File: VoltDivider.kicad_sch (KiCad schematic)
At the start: 4 parts, among them J4 Conn_01x01_Female

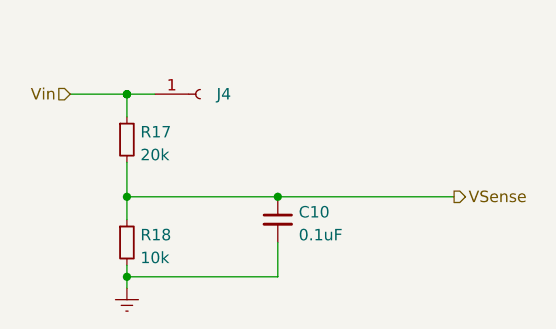
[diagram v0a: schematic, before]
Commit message: added new op amps and used automated traces due to complexity
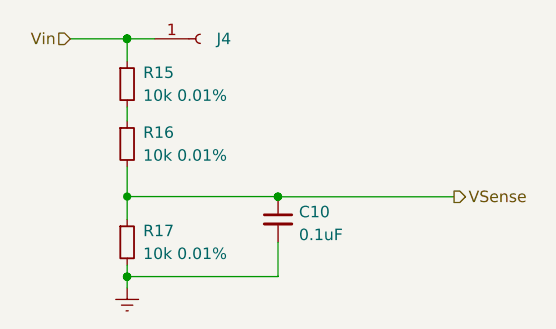
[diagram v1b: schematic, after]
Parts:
- added R16: 10k 0.01%, Resistor_SMD:R_0603_1608Metric, symbol Device:R_Small
- R15: renamed from R17; value 20k -> 10k 0.01%
- R17: renamed from R18; value 10k -> 10k 0.01%
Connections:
- net VSense: now also R16.2; no longer R15.2
- new net: R15.2, R16.1
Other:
- moved on the sheet: J4, R15
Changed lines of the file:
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@@
 (kicad_sch (version 20211123) (generator eeschema)
   (paper "A4")
-  (junction (at 134.0866 78.8162) (diameter 0) (color 0 0 0 0)
+  (junction (at 150.876 90.17) (diameter 0) (color 0 0 0 0)
   )
-  (junction (at 134.0866 90.1954) (diameter 0) (color 0 0 0 0)
+  (junction (at 134.0866 72.6694) (diameter 0) (color 0 0 0 0)
+  )
+  (junction (at 134.112 90.17) (diameter 0) (color 0 0 0 0)
   )
   (junction (at 134.0866 99.0854) (diameter 0) (color 0 0 0 0)
   )
-  (junction (at 134.0866 78.7908) (diameter 0) (color 0 0 0 0)
+  (junction (at 134.112 72.5932) (diameter 0) (color 0 0 0 0)
+  )
+  (junction (at 134.112 99.06) (diameter 0) (color 0 0 0 0)
+  )
+  (junction (at 134.0866 72.644) (diameter 0) (color 0 0 0 0)
   )
   (junction (at 150.8506 90.1954) (diameter 0) (color 0 0 0 0)
   )
-  (wire (pts (xy 134.0866 100.3554) (xy 134.0866 99.0854))
+  (wire (pts (xy 134.112 100.33) (xy 134.112 99.06))
     (stroke (width 0) (type default) (color 0 0 0 0))
   )
-  (wire (pts (xy 134.0866 78.8162) (xy 134.0866 81.3054))
+  (wire (pts (xy 134.112 80.2132) (xy 134.112 81.788))
+    (stroke (width 0) (type default) (color 0 0 0 0))
+  )
+  (wire (pts (xy 150.876 90.17) (xy 150.8506 90.1954))
+    (stroke (width 0) (type default) (color 0 0 0 0))
+  )
+  (wire (pts (xy 134.112 72.5932) (xy 134.112 75.1332))
     (stroke (width 0) (type default) (color 0 0 0 0))
   )
@@
     (stroke (width 0) (type default) (color 0 0 0 0))
   )
-  (wire (pts (xy 134.0866 90.1954) (xy 150.8506 90.1954))
+  (wire (pts (xy 134.112 99.06) (xy 134.0866 99.0854))
     (stroke (width 0) (type default) (color 0 0 0 0))
   )
-  (wire (pts (xy 137.16 78.7908) (xy 134.0866 78.7908))
+  (wire (pts (xy 134.112 90.17) (xy 150.876 90.17))
     (stroke (width 0) (type default) (color 0 0 0 0))
   )
-  (wire (pts (xy 150.8506 99.0854) (xy 150.8506 95.2754))
+  (wire (pts (xy 137.16 72.644) (xy 134.0866 72.644))
     (stroke (width 0) (type default) (color 0 0 0 0))
   )
-  (wire (pts (xy 134.0866 99.0854) (xy 150.8506 99.0854))
+  (wire (pts (xy 150.876 99.06) (xy 150.876 95.25))
     (stroke (width 0) (type default) (color 0 0 0 0))
   )
-  (wire (pts (xy 134.0866 90.1954) (xy 134.0866 86.3854))
+  (wire (pts (xy 134.112 86.868) (xy 134.112 90.17))
     (stroke (width 0) (type default) (color 0 0 0 0))
   )
-  (wire (pts (xy 127.7874 78.7908) (xy 134.0866 78.7908))
+  (wire (pts (xy 134.112 99.06) (xy 150.876 99.06))
     (stroke (width 0) (type default) (color 0 0 0 0))
   )
-  (wire (pts (xy 134.0866 78.8162) (xy 134.0866 78.7908))
+  (wire (pts (xy 134.112 72.5932) (xy 134.0866 72.6694))
     (stroke (width 0) (type default) (color 0 0 0 0))
   )
-  (wire (pts (xy 134.0866 92.7354) (xy 134.0866 90.1954))
+  (wire (pts (xy 127.7874 72.644) (xy 134.0866 72.644))
     (stroke (width 0) (type default) (color 0 0 0 0))
   )
-  (wire (pts (xy 134.0866 99.0854) (xy 134.0866 97.8154))
+  (wire (pts (xy 134.0866 72.6694) (xy 134.0866 72.644))
     (stroke (width 0) (type default) (color 0 0 0 0))
   )
-  (hierarchical_label "Vin" (shape input) (at 127.7874 78.7908 180)
+  (wire (pts (xy 134.112 92.71) (xy 134.112 90.17))
+    (stroke (width 0) (type default) (color 0 0 0 0))
+  )
+  (wire (pts (xy 134.112 99.06) (xy 134.112 97.79))
+    (stroke (width 0) (type default) (color 0 0 0 0))
+  )
+  (hierarchical_label "Vin" (shape input) (at 127.7874 72.644 180)
     (effects (font (size 1.27 1.27)) (justify right))
   )
@@
     (effects (font (size 1.27 1.27)) (justify left))
   )
-  (symbol (lib_id "Device:R_Small") (at 134.0866 95.2754 0) (unit 1)
+  (symbol (lib_id "Device:R_Small") (at 134.112 95.25 0) (unit 1)
     (in_bom yes) (on_board yes) (fields_autoplaced)
-    (property "Reference" "R18" (id 0) (at 135.5852 94.4407 0)
+    (property "Reference" "R17" (id 0) (at 135.89 93.9799 0)
       (effects (font (size 1.27 1.27)) (justify left))
     )
-    (property "Value" "10k" (id 1) (at 135.5852 96.9776 0)
+    (property "Value" "10k 0.01%" (id 1) (at 135.89 96.5199 0)
       (effects (font (size 1.27 1.27)) (justify left))
     )
-    (property "Footprint" "Resistor_SMD:R_0603_1608Metric" (id 2) (at 134.0866 95.2754 0)
+    (property "Footprint" "Resistor_SMD:R_0603_1608Metric" (id 2) (at 134.112 95.25 0)
       (effects (font (size 1.27 1.27)) hide)
     )
-    (property "Datasheet" "~" (id 3) (at 134.0866 95.2754 0)
+    (property "Datasheet" "~" (id 3) (at 134.112 95.25 0)
       (effects (font (size 1.27 1.27)) hide)
     )
@@
     (pin "2")
   )
-  (symbol (lib_id "Device:C_Small") (at 150.8506 92.7354 0) (unit 1)
+  (symbol (lib_id "Device:C_Small") (at 150.876 92.71 0) (unit 1)
     (in_bom yes) (on_board yes) (fields_autoplaced)
-    (property "Reference" "C10" (id 0) (at 153.1747 91.907 0)
+    (property "Reference" "C10" (id 0) (at 153.2001 91.8816 0)
       (effects (font (size 1.27 1.27)) (justify left))
     )
-    (property "Value" "0.1uF" (id 1) (at 153.1747 94.4439 0)
+    (property "Value" "0.1uF" (id 1) (at 153.2001 94.4185 0)
       (effects (font (size 1.27 1.27)) (justify left))
     )
-    (property "Footprint" "Capacitor_SMD:C_0603_1608Metric" (id 2) (at 150.8506 92.7354 0)
+    (property "Footprint" "Capacitor_SMD:C_0603_1608Metric" (id 2) (at 150.876 92.71 0)
       (effects (font (size 1.27 1.27)) hide)
     )
-    (property "Datasheet" "~" (id 3) (at 150.8506 92.7354 0)
+    (property "Datasheet" "~" (id 3) (at 150.876 92.71 0)
       (effects (font (size 1.27 1.27)) hide)
     )
@@
     (pin "2")
   )
-  (symbol (lib_id "Device:R_Small") (at 134.0866 83.8454 0) (unit 1)
+  (symbol (lib_id "Device:R_Small") (at 134.112 84.328 0) (unit 1)
     (in_bom yes) (on_board yes) (fields_autoplaced)
-    (property "Reference" "R17" (id 0) (at 135.5852 83.0107 0)
+    (property "Reference" "R16" (id 0) (at 135.89 83.0579 0)
       (effects (font (size 1.27 1.27)) (justify left))
     )
-    (property "Value" "20k" (id 1) (at 135.5852 85.5476 0)
+    (property "Value" "10k 0.01%" (id 1) (at 135.89 85.5979 0)
       (effects (font (size 1.27 1.27)) (justify left))
     )
-    (property "Footprint" "Resistor_SMD:R_0603_1608Metric" (id 2) (at 134.0866 83.8454 0)
+    (property "Footprint" "Resistor_SMD:R_0603_1608Metric" (id 2) (at 134.112 84.328 0)
       (effects (font (size 1.27 1.27)) hide)
     )
-    (property "Datasheet" "~" (id 3) (at 134.0866 83.8454 0)
+    (property "Datasheet" "~" (id 3) (at 134.112 84.328 0)
       (effects (font (size 1.27 1.27)) hide)
     )
@@
     (pin "2")
   )
-  (symbol (lib_id "Connector:Conn_01x01_Female") (at 142.24 78.7908 0) (unit 1)
+  (symbol (lib_id "Device:R_Small") (at 134.112 77.6732 0) (unit 1)
     (in_bom yes) (on_board yes) (fields_autoplaced)
-    (property "Reference" "J4" (id 0) (at 144.0434 78.7907 0)
+    (property "Reference" "R15" (id 0) (at 135.89 76.4031 0)
       (effects (font (size 1.27 1.27)) (justify left))
     )
-    (property "Value" "Conn_01x01_Female" (id 1) (at 142.9512 80.493 0)
+    (property "Value" "10k 0.01%" (id 1) (at 135.89 78.9431 0)
+      (effects (font (size 1.27 1.27)) (justify left))
+    )
+    (property "Footprint" "Resistor_SMD:R_0603_1608Metric" (id 2) (at 134.112 77.6732 0)
+      (effects (font (size 1.27 1.27)) hide)
+    )
+    (property "Datasheet" "~" (id 3) (at 134.112 77.6732 0)
+      (effects (font (size 1.27 1.27)) hide)
+    )
+    (pin "1")
+    (pin "2")
+  )
+  (symbol (lib_id "Connector:Conn_01x01_Female") (at 142.24 72.644 0) (unit 1)
+    (in_bom yes) (on_board yes) (fields_autoplaced)
+    (property "Reference" "J4" (id 0) (at 144.0434 72.6439 0)
+      (effects (font (size 1.27 1.27)) (justify left))
+    )
+    (property "Value" "Conn_01x01_Female" (id 1) (at 142.9512 74.3462 0)
       (effects (font (size 1.27 1.27)) (justify left) hide)
     )
-    (property "Footprint" "Connector_PinHeader_2.54mm:PinHeader_1x01_P2.54mm_Vertical" (id 2) (at 142.24 78.7908 0)
+    (property "Footprint" "Connector_PinHeader_2.54mm:PinHeader_1x01_P2.54mm_Vertical" (id 2) (at 142.24 72.644 0)
       (effects (font (size 1.27 1.27)) hide)
     )
-    (property "Datasheet" "~" (id 3) (at 142.24 78.7908 0)
+    (property "Datasheet" "~" (id 3) (at 142.24 72.644 0)
       (effects (font (size 1.27 1.27)) hide)
     )
     (pin "1")
   )
-  (symbol (lib_id "power:GNDREF") (at 134.0866 100.3554 0) (unit 1)
+  (symbol (lib_id "power:GNDREF") (at 134.112 100.33 0) (unit 1)
     (in_bom yes) (on_board yes) (fields_autoplaced)
-    (property "Reference" "#PWR010" (id 0) (at 134.0866 106.7054 0)
+    (property "Reference" "#PWR010" (id 0) (at 134.112 106.68 0)
       (effects (font (size 1.27 1.27)) hide)
     )
-    (property "Value" "GNDREF" (id 1) (at 134.0866 104.7988 0)
+    (property "Value" "GNDREF" (id 1) (at 134.112 104.7734 0)
       (effects (font (size 1.27 1.27)) hide)
     )
-    (property "Footprint" "" (id 2) (at 134.0866 100.3554 0)
+    (property "Footprint" "" (id 2) (at 134.112 100.33 0)
       (effects (font (size 1.27 1.27)) hide)
     )
-    (property "Datasheet" "" (id 3) (at 134.0866 100.3554 0)
+    (property "Datasheet" "" (id 3) (at 134.112 100.33 0)
       (effects (font (size 1.27 1.27)) hide)
     )

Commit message: new EMC-EMI layout with improved suppression
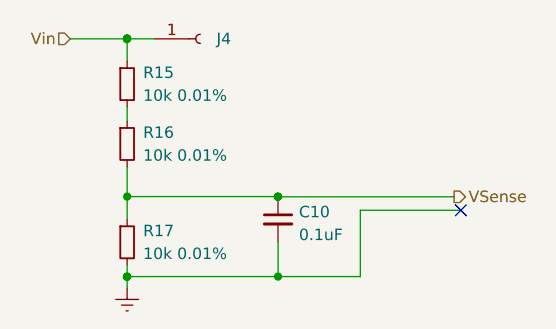
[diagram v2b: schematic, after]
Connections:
- no-connect marks 0 -> 1
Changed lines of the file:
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@@
   (junction (at 150.876 90.17) (diameter 0) (color 0 0 0 0)
+  )
+  (junction (at 150.876 99.06) (diameter 0) (color 0 0 0 0)
   )
   (junction (at 134.0866 72.6694) (diameter 0) (color 0 0 0 0)
@@
   (junction (at 150.8506 90.1954) (diameter 0) (color 0 0 0 0)
   )
+  (no_connect (at 171.196 91.694))
   (wire (pts (xy 134.112 100.33) (xy 134.112 99.06))
     (stroke (width 0) (type default) (color 0 0 0 0))
   )
   (wire (pts (xy 134.112 80.2132) (xy 134.112 81.788))
+    (stroke (width 0) (type default) (color 0 0 0 0))
+  )
+  (wire (pts (xy 160.02 91.694) (xy 171.196 91.694))
     (stroke (width 0) (type default) (color 0 0 0 0))
   )
@@
     (stroke (width 0) (type default) (color 0 0 0 0))
   )
+  (wire (pts (xy 150.876 99.06) (xy 160.02 99.06))
+    (stroke (width 0) (type default) (color 0 0 0 0))
+  )
   (wire (pts (xy 134.112 99.06) (xy 150.876 99.06))
     (stroke (width 0) (type default) (color 0 0 0 0))
@@
     (stroke (width 0) (type default) (color 0 0 0 0))
   )
+  (wire (pts (xy 160.02 99.06) (xy 160.02 91.694))
+    (stroke (width 0) (type default) (color 0 0 0 0))
+  )

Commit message: updates with foot print guard rings
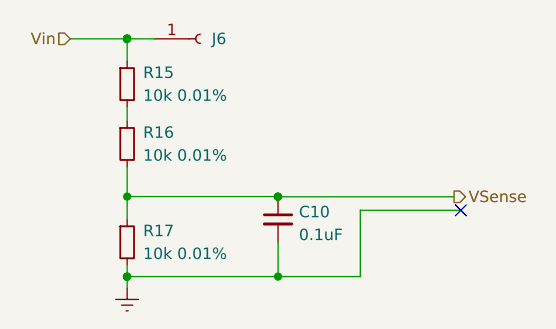
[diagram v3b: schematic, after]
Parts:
- renumbered J4 to J6
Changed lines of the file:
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@@
   (symbol (lib_id "Connector:Conn_01x01_Female") (at 142.24 72.644 0) (unit 1)
     (in_bom yes) (on_board yes) (fields_autoplaced)
-    (property "Reference" "J4" (id 0) (at 144.0434 72.6439 0)
+    (property "Reference" "J6" (id 0) (at 143.51 72.6439 0)
       (effects (font (size 1.27 1.27)) (justify left))
     )

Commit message: working on MUX and pre-amp layout
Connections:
- no-connect marks 1 -> 0
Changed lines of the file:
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@@
   (junction (at 150.876 90.17) (diameter 0) (color 0 0 0 0)
-  )
-  (junction (at 150.876 99.06) (diameter 0) (color 0 0 0 0)
   )
   (junction (at 134.0866 72.6694) (diameter 0) (color 0 0 0 0)
@@
   (junction (at 150.8506 90.1954) (diameter 0) (color 0 0 0 0)
   )
-  (no_connect (at 171.196 91.694))
   (wire (pts (xy 134.112 100.33) (xy 134.112 99.06))
     (stroke (width 0) (type default) (color 0 0 0 0))
   )
   (wire (pts (xy 134.112 80.2132) (xy 134.112 81.788))
-    (stroke (width 0) (type default) (color 0 0 0 0))
-  )
-  (wire (pts (xy 160.02 91.694) (xy 171.196 91.694))
     (stroke (width 0) (type default) (color 0 0 0 0))
   )
@@
     (stroke (width 0) (type default) (color 0 0 0 0))
   )
-  (wire (pts (xy 150.876 99.06) (xy 160.02 99.06))
-    (stroke (width 0) (type default) (color 0 0 0 0))
-  )
   (wire (pts (xy 134.112 99.06) (xy 150.876 99.06))
     (stroke (width 0) (type default) (color 0 0 0 0))
@@
     (stroke (width 0) (type default) (color 0 0 0 0))
   )
-  (wire (pts (xy 160.02 99.06) (xy 160.02 91.694))
-    (stroke (width 0) (type default) (color 0 0 0 0))
-  )
